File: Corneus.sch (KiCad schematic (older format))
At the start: 145 parts, among them J1 USB_B_Micro, Q1 Q_NPN_BCE, SW1 SW_Push, U1 ATmega32U4-AU, U2 PRTR5V0U2X, Y1 16MHz

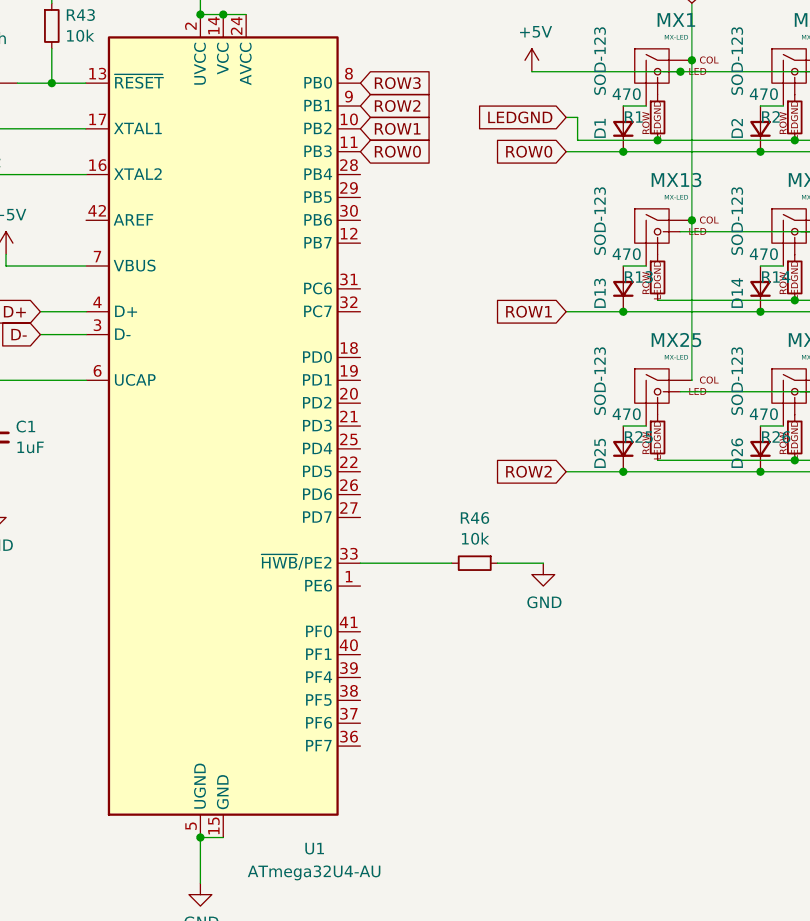
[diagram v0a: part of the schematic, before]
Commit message: rerouted columns
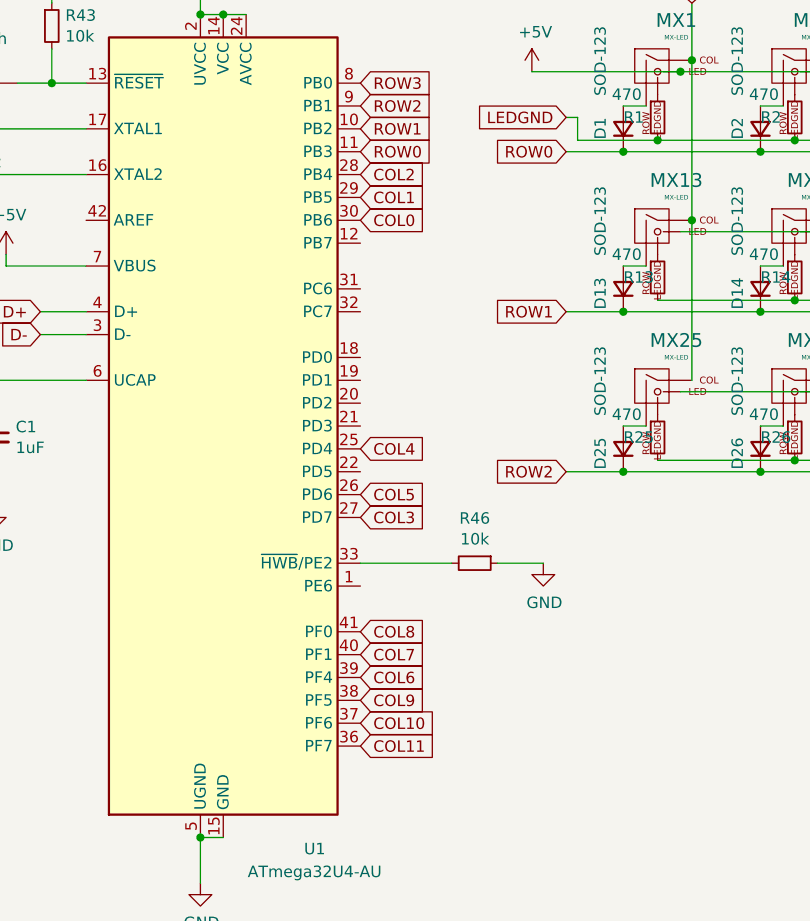
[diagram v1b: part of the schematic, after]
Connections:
- net COL0: now also U1.30 (PB6)
- net COL1: now also U1.29 (PB5)
- net COL10: now also U1.37 (PF6)
- net COL11: now also U1.36 (PF7)
- net COL2: now also U1.28 (PB4)
- net COL3: now also U1.27 (PD7)
- net COL4: now also U1.25 (PD4)
- net COL5: now also U1.26 (PD6)
- net COL6: now also U1.39 (PF4)
- net COL7: now also U1.40 (PF1)
- net COL8: now also U1.41 (PF0)
- net COL9: now also U1.38 (PF5)
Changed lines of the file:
@@
 Text GLabel 2950 1450 2    50   Input ~ 0
 ROW0
+Text GLabel 2950 2750 2    50   Input ~ 0
+COL4
+Text GLabel 2950 2950 2    50   Input ~ 0
+COL5
+Text GLabel 2950 3050 2    50   Input ~ 0
+COL3
+Text GLabel 2950 1550 2    50   Input ~ 0
+COL2
+Text GLabel 2950 1650 2    50   Input ~ 0
+COL1
+Text GLabel 2950 1750 2    50   Input ~ 0
+COL0
+Text GLabel 2950 3750 2    50   Input ~ 0
+COL6
+Text GLabel 2950 3650 2    50   Input ~ 0
+COL7
+Text GLabel 2950 3550 2    50   Input ~ 0
+COL8
+Text GLabel 2950 3850 2    50   Input ~ 0
+COL9
+Text GLabel 2950 3950 2    50   Input ~ 0
+COL10
+Text GLabel 2950 4050 2    50   Input ~ 0
+COL11
 $EndSCHEMATC

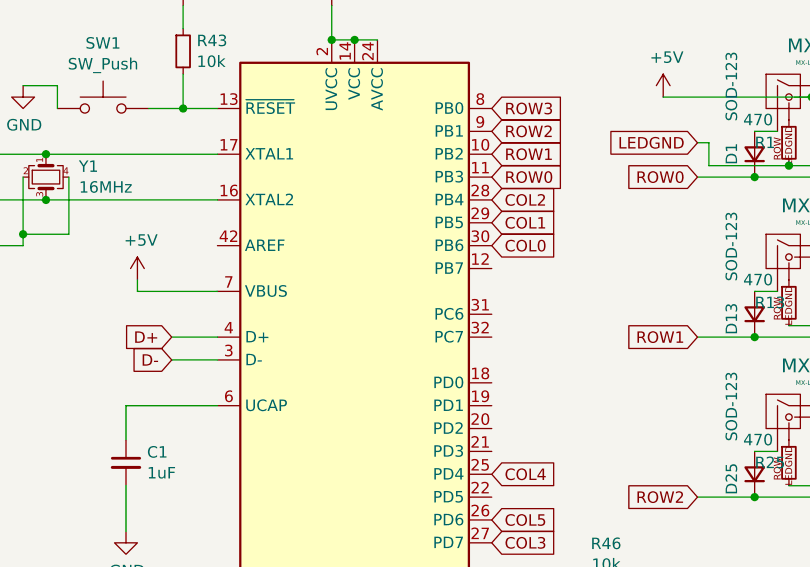
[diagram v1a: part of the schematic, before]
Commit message: add ground fills, adjust some traces to improve clearance
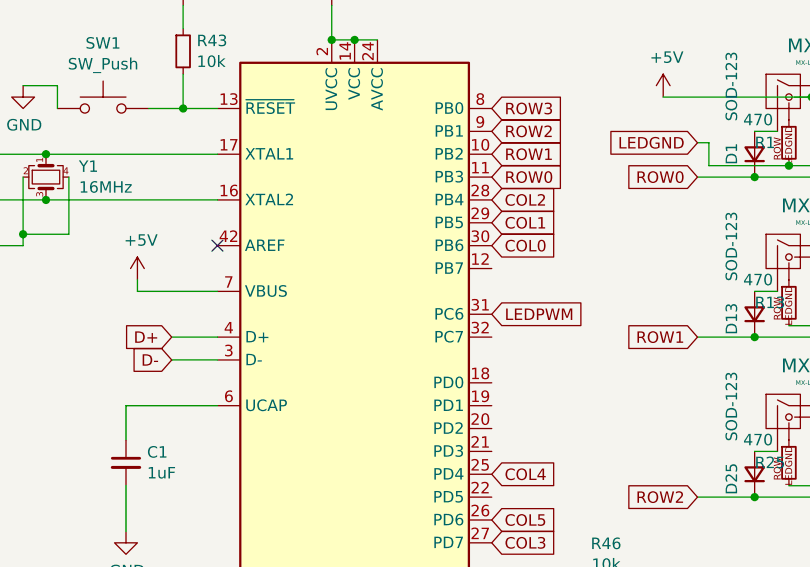
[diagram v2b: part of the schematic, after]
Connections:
- net LEDPWM: now also U1.31 (PC6)
- no-connect marks 1 -> 2
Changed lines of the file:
@@
 Text GLabel 2950 4050 2    50   Input ~ 0
 COL11
+Text GLabel 2950 2050 2    50   Input ~ 0
+LEDPWM
+NoConn ~ 1750 1750
 $EndSCHEMATC
